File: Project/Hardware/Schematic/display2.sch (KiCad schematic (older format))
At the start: 11 parts

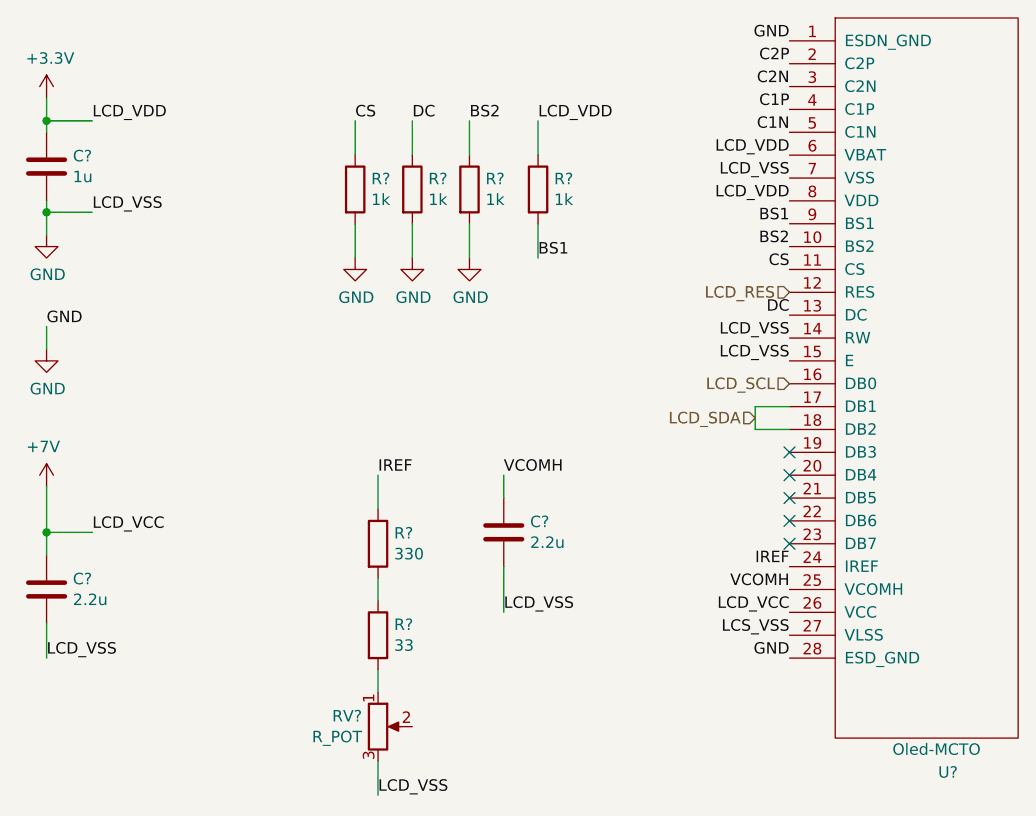
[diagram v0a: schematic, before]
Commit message: La till en till display och fixa fel
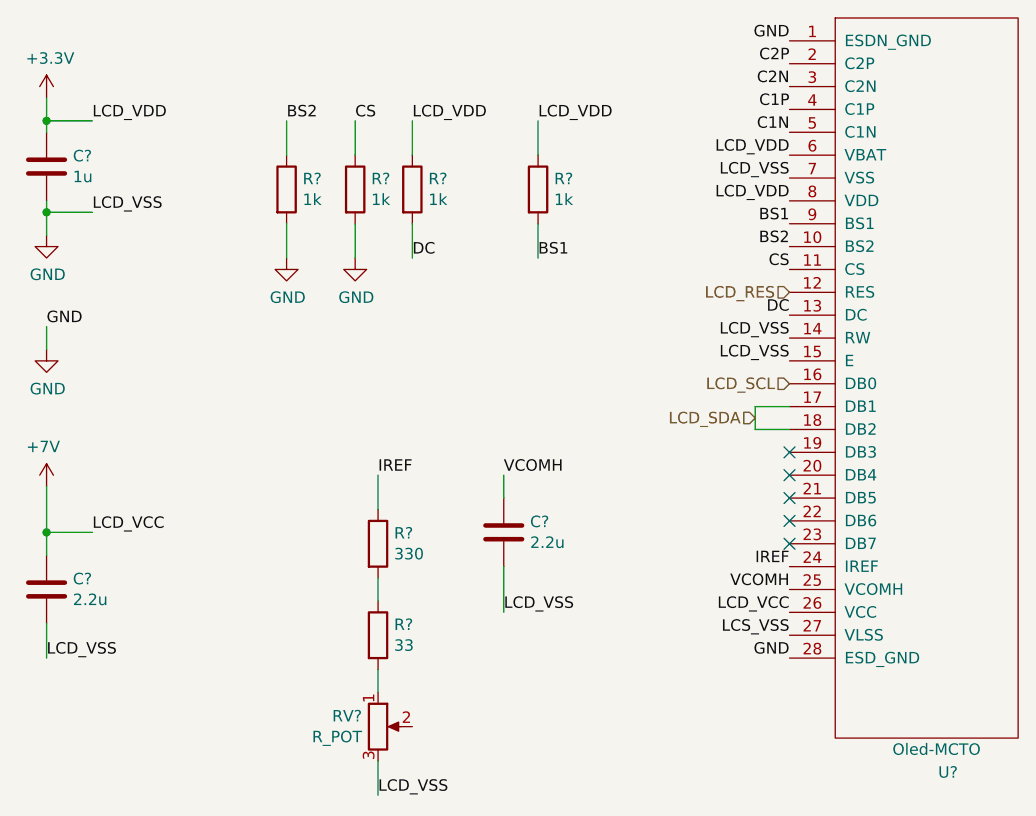
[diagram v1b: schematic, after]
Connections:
- net +3V3: now also R?.1
- net DC: now also R?.2; no longer R?.1
- net GND: no longer R?.2
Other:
- moved on the sheet: R?
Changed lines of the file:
@@
 $Descr User 5906 5906
 encoding utf-8
-Sheet 5 8
+Sheet 8 8
 Title ""
 Date ""
@@
 L Device:R R?
 U 1 1 5C67D7C1
-P 2700 1400
+P 1900 1400
 AR Path="/5C564F2E/5C67D7C1" Ref="R?"  Part="1"
 AR Path="/5C5FFA20/5C67D7C1" Ref="R?"  Part="1"
-F 0 "R?" H 2770 1446 50  0000 L CNN
-F 1 "1k" H 2770 1355 50  0000 L CNN
-F 2 "" V 2630 1400 50  0001 C CNN
-F 3 "~" H 2700 1400 50  0001 C CNN
-	1    2700 1400
-	1    0    0    -1
-$EndComp
-Wire Wire Line
-	2700 1250 2700 1100
-Text Label 2700 1100 0    50   ~ 0
+F 0 "R?" H 1970 1446 50  0000 L CNN
+F 1 "1k" H 1970 1355 50  0000 L CNN
+F 2 "" V 1830 1400 50  0001 C CNN
+F 3 "~" H 1900 1400 50  0001 C CNN
+	1    1900 1400
+	1    0    0    -1
+$EndComp
+Wire Wire Line
+	1900 1250 1900 1100
+Text Label 1900 1100 0    50   ~ 0
 BS2
-$Comp
-L power:GND #PWR?
-U 1 1 5C67D9C3
-P 2450 1700
-AR Path="/5C564F2E/5C67D9C3" Ref="#PWR?"  Part="1"
-AR Path="/5C5FFA20/5C67D9C3" Ref="#PWR?"  Part="1"
-F 0 "#PWR?" H 2450 1450 50  0001 C CNN
-F 1 "GND" H 2455 1527 50  0000 C CNN
-F 2 "" H 2450 1700 50  0001 C CNN
-F 3 "" H 2450 1700 50  0001 C CNN
-	1    2450 1700
-	1    0    0    -1
-$EndComp
 Wire Wire Line
 	2450 1550 2450 1700
@@
 L power:GND #PWR?
 U 1 1 5C67E539
-P 2700 1700
+P 1900 1700
 AR Path="/5C564F2E/5C67E539" Ref="#PWR?"  Part="1"
 AR Path="/5C5FFA20/5C67E539" Ref="#PWR?"  Part="1"
-F 0 "#PWR?" H 2700 1450 50  0001 C CNN
-F 1 "GND" H 2705 1527 50  0000 C CNN
-F 2 "" H 2700 1700 50  0001 C CNN
-F 3 "" H 2700 1700 50  0001 C CNN
-	1    2700 1700
-	1    0    0    -1
-$EndComp
-Wire Wire Line
-	2700 1700 2700 1550
+F 0 "#PWR?" H 1900 1450 50  0001 C CNN
+F 1 "GND" H 1905 1527 50  0000 C CNN
+F 2 "" H 1900 1700 50  0001 C CNN
+F 3 "" H 1900 1700 50  0001 C CNN
+	1    1900 1700
+	1    0    0    -1
+$EndComp
+Wire Wire Line
+	1900 1700 1900 1550
 Wire Wire Line
 	2450 1250 2450 1100
-Text Label 2450 1100 0    50   ~ 0
+Text Label 2450 1700 0    50   ~ 0
 DC
 Text Label 4100 1950 2    50   ~ 0
@@
 Text Label 850  3450 0    50   ~ 0
 LCD_VSS
+Text Label 2450 1100 0    50   ~ 0
+LCD_VDD
 Text Label 4100 2150 2    50   ~ 0
 LCD_VSS
@@
 $Comp
 L PASC:+7V #PWR?
-U 1 1 5C646FD1
+U 1 1 5C645DB7
 P 850 2700
 F 0 "#PWR?" H 1100 2800 50  0001 C CNN
